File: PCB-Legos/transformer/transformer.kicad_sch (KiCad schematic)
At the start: 3 parts, among them J1 Conn_Coaxial, U1 NCS3-272+

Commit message: fixed SMA connector footprint, moved text from paste to silk layer
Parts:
- J1: footprint HGS_Reflector:132134-10 -> Footprints:J-Amphenol-132134-10-SMA-F-SMT-vertical
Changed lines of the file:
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@@
     (property "Reference" "J1" (id 0) (at 115.8874 78.74 0))
     (property "Value" "Conn_Coaxial" (id 1) (at 115.8874 81.28 0))
-    (property "Footprint" "HGS_Reflector:132134-10" (id 2) (at 115.57 86.36 0)
+    (property "Footprint" "Footprints:J-Amphenol-132134-10-SMA-F-SMT-vertical" (id 2) (at 115.57 86.36 0)
       (effects (font (size 1.27 1.27)) hide)
     )
@@
     )
     (path "/2dd0add1-9a95-4b8c-a47a-bb7c827bbb1c"
-      (reference "J1") (unit 1) (value "Conn_Coaxial") (footprint "HGS_Reflector:132134-10")
+      (reference "J1") (unit 1) (value "Conn_Coaxial") (footprint "Footprints:J-Amphenol-132134-10-SMA-F-SMT-vertical")
     )
     (path "/8a429765-4e67-4a49-8e8d-ddb3e75fdadd"

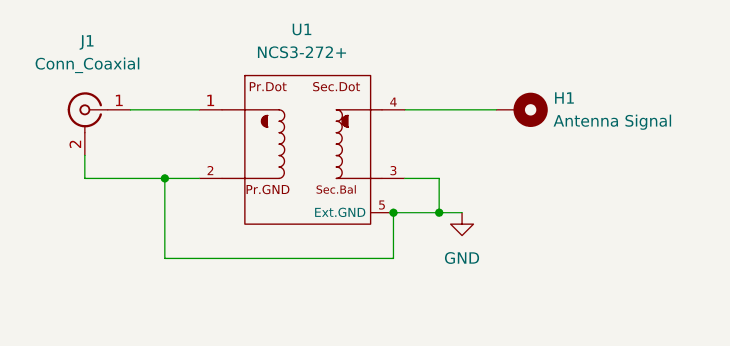
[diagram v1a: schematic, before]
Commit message: Sent off for Fab, v1.0
Updated libraries and library paths; might actually not be terrible now with the submodule? Fixed footprint of transformer and rotated 90 degrees; made board OCD compliant and did via cleanup.
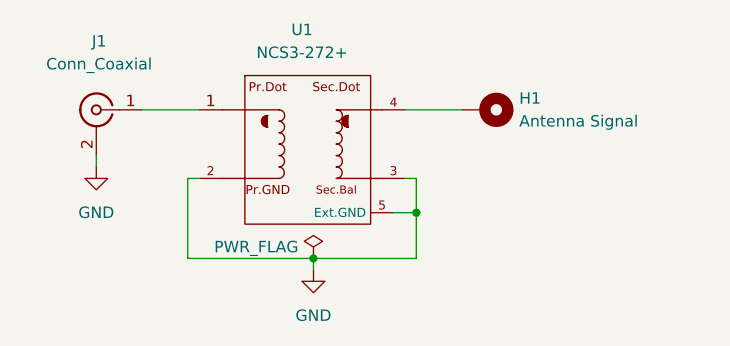
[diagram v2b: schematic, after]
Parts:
- J1: footprint Footprints:J-Amphenol-132134-10-SMA-F-SMT-vertical -> footprints:J-Amphenol-132134-10-SMA-F-SMT-vertical
- U1: footprint NCS3-272+:FIL_MEM2012SC470 -> footprints:Minicircuits-GE0805C-9; symbol NCS3_272:NCS3-272+ -> U-Minicircuits-NCS3-272+-ceramic-transformer:NCS3-272+
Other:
- moved on the sheet: H1, J1
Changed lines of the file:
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@@
 (kicad_sch (version 20211123) (generator eeschema)
   (paper "A4")
-  (junction (at 149.86 97.79) (diameter 0) (color 0 0 0 0)
+  (junction (at 140.97 102.87) (diameter 0) (color 0 0 0 0)
   )
-  (junction (at 154.94 97.79) (diameter 0) (color 0 0 0 0)
+  (junction (at 152.4 97.79) (diameter 0) (color 0 0 0 0)
   )
-  (junction (at 124.46 93.98) (diameter 0) (color 0 0 0 0)
-  )
-  (wire (pts (xy 120.65 86.36) (xy 128.27 86.36))
+  (wire (pts (xy 121.92 86.36) (xy 128.27 86.36))
     (stroke (width 0) (type default) (color 0 0 0 0))
   )
-  (wire (pts (xy 124.46 102.87) (xy 149.86 102.87))
+  (wire (pts (xy 127 93.98) (xy 128.27 93.98))
     (stroke (width 0) (type default) (color 0 0 0 0))
   )
-  (wire (pts (xy 115.57 93.98) (xy 124.46 93.98))
+  (wire (pts (xy 140.97 102.87) (xy 140.97 104.14))
     (stroke (width 0) (type default) (color 0 0 0 0))
   )
-  (wire (pts (xy 154.94 97.79) (xy 157.48 97.79))
+  (wire (pts (xy 127 102.87) (xy 140.97 102.87))
     (stroke (width 0) (type default) (color 0 0 0 0))
   )
-  (wire (pts (xy 151.13 86.36) (xy 161.29 86.36))
+  (wire (pts (xy 151.13 86.36) (xy 157.48 86.36))
     (stroke (width 0) (type default) (color 0 0 0 0))
   )
-  (wire (pts (xy 151.13 93.98) (xy 154.94 93.98))
+  (wire (pts (xy 140.97 102.87) (xy 152.4 102.87))
     (stroke (width 0) (type default) (color 0 0 0 0))
   )
-  (wire (pts (xy 124.46 93.98) (xy 124.46 102.87))
+  (wire (pts (xy 151.13 93.98) (xy 152.4 93.98))
     (stroke (width 0) (type default) (color 0 0 0 0))
   )
-  (wire (pts (xy 154.94 93.98) (xy 154.94 97.79))
+  (wire (pts (xy 127 93.98) (xy 127 102.87))
     (stroke (width 0) (type default) (color 0 0 0 0))
   )
-  (wire (pts (xy 149.86 97.79) (xy 149.86 102.87))
+  (wire (pts (xy 149.86 97.79) (xy 152.4 97.79))
     (stroke (width 0) (type default) (color 0 0 0 0))
   )
-  (wire (pts (xy 149.86 97.79) (xy 154.94 97.79))
+  (wire (pts (xy 152.4 93.98) (xy 152.4 97.79))
     (stroke (width 0) (type default) (color 0 0 0 0))
   )
-  (wire (pts (xy 115.57 91.44) (xy 115.57 93.98))
+  (wire (pts (xy 116.84 91.44) (xy 116.84 92.71))
     (stroke (width 0) (type default) (color 0 0 0 0))
   )
-  (wire (pts (xy 124.46 93.98) (xy 128.27 93.98))
+  (wire (pts (xy 152.4 97.79) (xy 152.4 102.87))
     (stroke (width 0) (type default) (color 0 0 0 0))
   )
-  (symbol (lib_id "Connector:Conn_Coaxial") (at 115.57 86.36 0) (mirror y) (unit 1)
+  (symbol (lib_id "Connector:Conn_Coaxial") (at 116.84 86.36 0) (mirror y) (unit 1)
     (in_bom yes) (on_board yes) (fields_autoplaced)
-    (property "Reference" "J1" (id 0) (at 115.8874 78.74 0))
-    (property "Value" "Conn_Coaxial" (id 1) (at 115.8874 81.28 0))
-    (property "Footprint" "Footprints:J-Amphenol-132134-10-SMA-F-SMT-vertical" (id 2) (at 115.57 86.36 0)
+    (property "Reference" "J1" (id 0) (at 117.1574 78.74 0))
+    (property "Value" "Conn_Coaxial" (id 1) (at 117.1574 81.28 0))
+    (property "Footprint" "footprints:J-Amphenol-132134-10-SMA-F-SMT-vertical" (id 2) (at 116.84 86.36 0)
       (effects (font (size 1.27 1.27)) hide)
     )
-    (property "Datasheet" " ~" (id 3) (at 115.57 86.36 0)
+    (property "Datasheet" " ~" (id 3) (at 116.84 86.36 0)
       (effects (font (size 1.27 1.27)) hide)
     )
@@
     (pin "2")
   )
-  (symbol (lib_name "NCS3-272+_1") (lib_id "NCS3_272:NCS3-272+") (at 140.97 93.98 0) (unit 1)
+  (symbol (lib_id "power:PWR_FLAG") (at 140.97 102.87 0) (unit 1)
+    (in_bom yes) (on_board yes)
+    (property "Reference" "#FLG01" (id 0) (at 140.97 100.965 0)
+      (effects (font (size 1.27 1.27)) hide)
+    )
+    (property "Value" "PWR_FLAG" (id 1) (at 134.62 101.6 0))
+    (property "Footprint" "" (id 2) (at 140.97 102.87 0)
+      (effects (font (size 1.27 1.27)) hide)
+    )
+    (property "Datasheet" "~" (id 3) (at 140.97 102.87 0)
+      (effects (font (size 1.27 1.27)) hide)
+    )
+    (pin "1")
+  )
+  (symbol (lib_id "U-Minicircuits-NCS3-272+-ceramic-transformer:NCS3-272+") (at 140.97 93.98 0) (unit 1)
     (in_bom yes) (on_board yes) (fields_autoplaced)
     (property "Reference" "U1" (id 0) (at 139.7 77.47 0))
     (property "Value" "NCS3-272+" (id 1) (at 139.7 80.01 0))
-    (property "Footprint" "NCS3-272+:FIL_MEM2012SC470" (id 2) (at 140.97 93.98 0)
+    (property "Footprint" "footprints:Minicircuits-GE0805C-9" (id 2) (at 140.97 93.98 0)
       (effects (font (size 1.27 1.27)) hide)
     )
-    (property "Datasheet" "" (id 3) (at 140.97 93.98 0)
+    (property "Datasheet" "https://www.minicircuits.com/pdfs/NCS3-272+.pdf" (id 3) (at 140.97 101.6 0)
       (effects (font (size 1.27 1.27)) hide)
     )
@@
     (pin "5")
   )
-  (symbol (lib_id "Mechanical:MountingHole_Pad") (at 163.83 86.36 270) (unit 1)
+  (symbol (lib_id "Mechanical:MountingHole_Pad") (at 160.02 86.36 270) (unit 1)
     (in_bom yes) (on_board yes) (fields_autoplaced)
-    (property "Reference" "H1" (id 0) (at 167.64 85.0899 90)
+    (property "Reference" "H1" (id 0) (at 163.83 85.0899 90)
       (effects (font (size 1.27 1.27)) (justify left))
     )
-    (property "Value" "Antenna Signal" (id 1) (at 167.64 87.6299 90)
+    (property "Value" "Antenna Signal" (id 1) (at 163.83 87.6299 90)
       (effects (font (size 1.27 1.27)) (justify left))
     )
-    (property "Footprint" "Connector_Pin:Pin_D1.0mm_L10.0mm" (id 2) (at 163.83 86.36 0)
+    (property "Footprint" "Connector_Pin:Pin_D1.0mm_L10.0mm" (id 2) (at 160.02 86.36 0)
       (effects (font (size 1.27 1.27)) hide)
     )
-    (property "Datasheet" "~" (id 3) (at 163.83 86.36 0)
+    (property "Datasheet" "~" (id 3) (at 160.02 86.36 0)
       (effects (font (size 1.27 1.27)) hide)
     )
     (pin "1")
   )
-  (symbol (lib_id "power:GND") (at 157.48 97.79 0) (unit 1)
+  (symbol (lib_id "power:GND") (at 140.97 104.14 0) (unit 1)
     (in_bom yes) (on_board yes) (fields_autoplaced)
-    (property "Reference" "#PWR0101" (id 0) (at 157.48 104.14 0)
+    (property "Reference" "#PWR02" (id 0) (at 140.97 110.49 0)
       (effects (font (size 1.27 1.27)) hide)
     )
-    (property "Value" "GND" (id 1) (at 157.48 102.87 0))
-    (property "Footprint" "" (id 2) (at 157.48 97.79 0)
+    (property "Value" "GND" (id 1) (at 140.97 109.22 0))
+    (property "Footprint" "" (id 2) (at 140.97 104.14 0)
       (effects (font (size 1.27 1.27)) hide)
     )
-    (property "Datasheet" "" (id 3) (at 157.48 97.79 0)
+    (property "Datasheet" "" (id 3) (at 140.97 104.14 0)
+      (effects (font (size 1.27 1.27)) hide)
+    )
+    (pin "1")
+  )
+  (symbol (lib_id "power:GND") (at 116.84 92.71 0) (unit 1)
+    (in_bom yes) (on_board yes) (fields_autoplaced)
+    (property "Reference" "#PWR01" (id 0) (at 116.84 99.06 0)
+      (effects (font (size 1.27 1.27)) hide)
+    )
+    (property "Value" "GND" (id 1) (at 116.84 97.79 0))
+    (property "Footprint" "" (id 2) (at 116.84 92.71 0)
+      (effects (font (size 1.27 1.27)) hide)
+    )
+    (property "Datasheet" "" (id 3) (at 116.84 92.71 0)
       (effects (font (size 1.27 1.27)) hide)
     )
@@
   )
   (symbol_instances
+    (path "/42df0aa5-95ee-4285-88f5-dbb30410b3cd"
+      (reference "#FLG01") (unit 1) (value "PWR_FLAG") (footprint "")
+    )
+    (path "/ee910aec-70e9-4f16-96e4-d98b11ee7154"
+      (reference "#PWR01") (unit 1) (value "GND") (footprint "")
+    )
     (path "/ddcc0092-f2f1-43c5-95f5-7a375fcd3638"
-      (reference "#PWR0101") (unit 1) (value "GND") (footprint "")
+      (reference "#PWR02") (unit 1) (value "GND") (footprint "")
     )
     (path "/dafc2fb0-df9a-4c90-8250-b9fdfd2b6008"
@@
     )
     (path "/2dd0add1-9a95-4b8c-a47a-bb7c827bbb1c"
-      (reference "J1") (unit 1) (value "Conn_Coaxial") (footprint "Footprints:J-Amphenol-132134-10-SMA-F-SMT-vertical")
+      (reference "J1") (unit 1) (value "Conn_Coaxial") (footprint "footprints:J-Amphenol-132134-10-SMA-F-SMT-vertical")
     )
     (path "/8a429765-4e67-4a49-8e8d-ddb3e75fdadd"
-      (reference "U1") (unit 1) (value "NCS3-272+") (footprint "NCS3-272+:FIL_MEM2012SC470")
+      (reference "U1") (unit 1) (value "NCS3-272+") (footprint "footprints:Minicircuits-GE0805C-9")
     )
   )

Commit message: Updated library paths to be more sane, especially for footprints. Then unmasked the vias along the edges so that we can get castellated edges. Also reduced the size of the antenna hole, no reason to be that big.
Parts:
- H1: footprint Connector_Pin:Pin_D1.0mm_L10.0mm -> Connector_Pin:Pin_D0.7mm_L6.5mm_W1.8mm_FlatFork
- J1: footprint footprints:J-Amphenol-132134-10-SMA-F-SMT-vertical -> oresat-footprints:J-Amphenol-132134-10-SMA-F-SMT-vertical
- U1: footprint footprints:Minicircuits-GE0805C-9 -> oresat-footprints:U-Minicircuits-GE0805C-9
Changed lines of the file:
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@@
     (property "Reference" "J1" (id 0) (at 117.1574 78.74 0))
     (property "Value" "Conn_Coaxial" (id 1) (at 117.1574 81.28 0))
-    (property "Footprint" "footprints:J-Amphenol-132134-10-SMA-F-SMT-vertical" (id 2) (at 116.84 86.36 0)
+    (property "Footprint" "oresat-footprints:J-Amphenol-132134-10-SMA-F-SMT-vertical" (id 2) (at 116.84 86.36 0)
       (effects (font (size 1.27 1.27)) hide)
     )
@@
     (property "Reference" "U1" (id 0) (at 139.7 77.47 0))
     (property "Value" "NCS3-272+" (id 1) (at 139.7 80.01 0))
-    (property "Footprint" "footprints:Minicircuits-GE0805C-9" (id 2) (at 140.97 93.98 0)
+    (property "Footprint" "oresat-footprints:U-Minicircuits-GE0805C-9" (id 2) (at 140.97 93.98 0)
       (effects (font (size 1.27 1.27)) hide)
     )
@@
       (effects (font (size 1.27 1.27)) (justify left))
     )
-    (property "Footprint" "Connector_Pin:Pin_D1.0mm_L10.0mm" (id 2) (at 160.02 86.36 0)
+    (property "Footprint" "Connector_Pin:Pin_D0.7mm_L6.5mm_W1.8mm_FlatFork" (id 2) (at 160.02 86.36 0)
       (effects (font (size 1.27 1.27)) hide)
     )
@@
     )
     (path "/dafc2fb0-df9a-4c90-8250-b9fdfd2b6008"
-      (reference "H1") (unit 1) (value "Antenna Signal") (footprint "Connector_Pin:Pin_D1.0mm_L10.0mm")
+      (reference "H1") (unit 1) (value "Antenna Signal") (footprint "Connector_Pin:Pin_D0.7mm_L6.5mm_W1.8mm_FlatFork")
     )
     (path "/2dd0add1-9a95-4b8c-a47a-bb7c827bbb1c"
-      (reference "J1") (unit 1) (value "Conn_Coaxial") (footprint "footprints:J-Amphenol-132134-10-SMA-F-SMT-vertical")
+      (reference "J1") (unit 1) (value "Conn_Coaxial") (footprint "oresat-footprints:J-Amphenol-132134-10-SMA-F-SMT-vertical")
     )
     (path "/8a429765-4e67-4a49-8e8d-ddb3e75fdadd"
-      (reference "U1") (unit 1) (value "NCS3-272+") (footprint "footprints:Minicircuits-GE0805C-9")
+      (reference "U1") (unit 1) (value "NCS3-272+") (footprint "oresat-footprints:U-Minicircuits-GE0805C-9")
     )
   )
